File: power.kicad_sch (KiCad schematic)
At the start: 57 parts, among them J4 USB_C_Receptacle_USB2.0_16P, Q5 AO3401A, Q6 2N7002, SW1 SW_Push, U10 BQ27441DRZR-G1A, U5 XL4005, U6 IP5306, U8 FP6298XR, U9 AMS1117-3.3

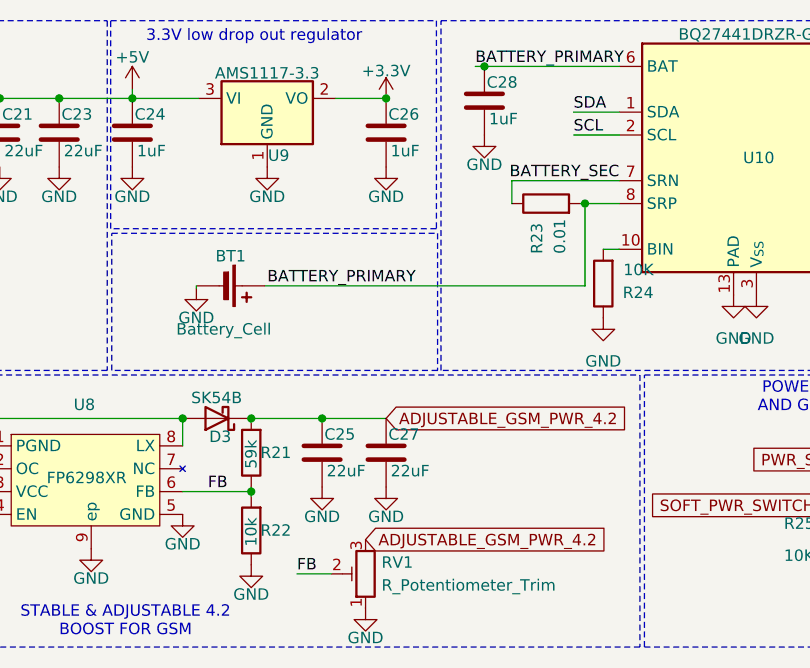
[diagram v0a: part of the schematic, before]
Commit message: cleaned up more routing and component placement
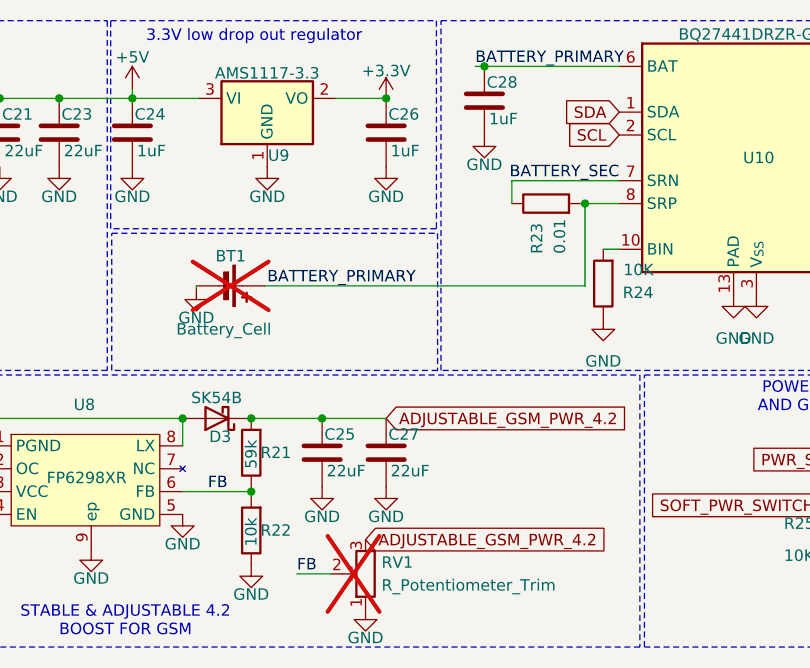
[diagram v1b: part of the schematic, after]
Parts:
- BT1, RV1: now not fitted
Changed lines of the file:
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@@
 	(wire
 		(pts
-			(xy 219.202 22.352) (xy 224.282 22.352)
-		)
-		(stroke
-			(width 0)
-			(type default)
-		)
-	)
-	(wire
-		(pts
 			(xy 132.842 64.77) (xy 132.842 61.976)
 		)
@@
 	(wire
 		(pts
-			(xy 219.202 24.892) (xy 224.282 24.892)
-		)
-		(stroke
-			(width 0)
-			(type default)
-		)
-	)
-	(wire
-		(pts
 			(xy 253.238 60.96) (xy 255.016 60.96)
 		)
@@
 		)
 	)
-	(label "SDA"
-		(at 219.202 22.352 0)
-		(effects
-			(font
-				(size 1.27 1.27)
-			)
-			(justify left bottom)
-		)
-	)
 	(label "VIN"
 		(at 83.058 20.828 0)
@@
 		)
 	)
-	(label "SCL"
-		(at 219.202 24.892 0)
-		(effects
-			(font
-				(size 1.27 1.27)
-			)
-			(justify left bottom)
-		)
-	)
 	(label "BATTERY_PRIMARY"
 		(at 208.28 17.272 0)
@@
 		)
 	)
+	(global_label "SDA"
+		(shape input)
+		(at 224.282 22.352 180)
+		(fields_autoplaced yes)
+		(effects
+			(font
+				(size 1.27 1.27)
+			)
+			(justify right)
+		)
+		(property "Intersheetrefs" "${INTERSHEET_REFS}"
+			(at 217.7287 22.352 0)
+			(effects
+				(font
+					(size 1.27 1.27)
+				)
+				(justify right)
+				(hide yes)
+			)
+		)
+	)
 	(global_label "GSM_PWR_EN"
 		(shape input)
@@
 		)
 	)
+	(global_label "SCL"
+		(shape input)
+		(at 224.282 24.892 180)
+		(fields_autoplaced yes)
+		(effects
+			(font
+				(size 1.27 1.27)
+			)
+			(justify right)
+		)
+		(property "Intersheetrefs" "${INTERSHEET_REFS}"
+			(at 217.7892 24.892 0)
+			(effects
+				(font
+					(size 1.27 1.27)
+				)
+				(justify right)
+				(hide yes)
+			)
+		)
+	)
 	(global_label "CC1"
 		(shape input)
@@
 		(exclude_from_sim yes)
 		(in_bom no)
-		(on_board yes)
+		(on_board no)
 		(dnp no)
 		(fields_autoplaced yes)
@@
 		(exclude_from_sim yes)
 		(in_bom no)
-		(on_board yes)
+		(on_board no)
 		(dnp no)
 		(fields_autoplaced yes)
@@
 		(exclude_from_sim no)
 		(in_bom yes)
-		(on_board yes)
-		(dnp no)
+		(on_board no)
+		(dnp yes)
 		(fields_autoplaced yes)
 		(property "Reference" "RV1"
@@
 		(exclude_from_sim yes)
 		(in_bom no)
-		(on_board yes)
+		(on_board no)
 		(dnp no)
 		(fields_autoplaced yes)
@@
 		(exclude_from_sim yes)
 		(in_bom no)
-		(on_board yes)
+		(on_board no)
 		(dnp no)
 		(fields_autoplaced yes)
@@
 		(exclude_from_sim no)
 		(in_bom yes)
-		(on_board yes)
-		(dnp no)
+		(on_board no)
+		(dnp yes)
 		(property "Reference" "BT1"
 			(at 181.102 38.354 90)

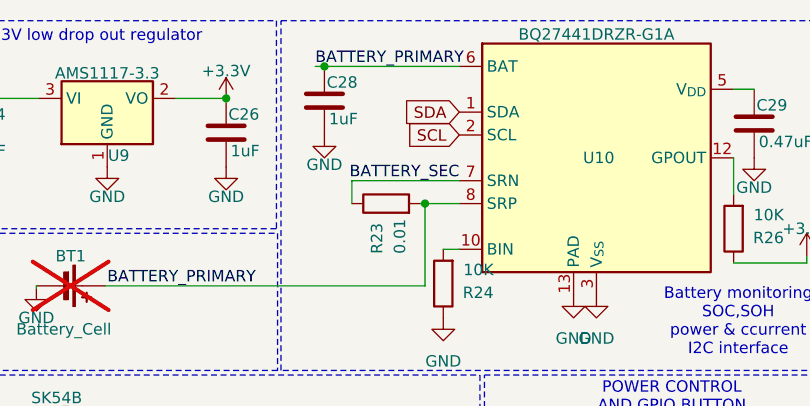
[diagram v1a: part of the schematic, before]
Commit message: added 3.3v logic level  shifting for battery monitoring chip I2C lines
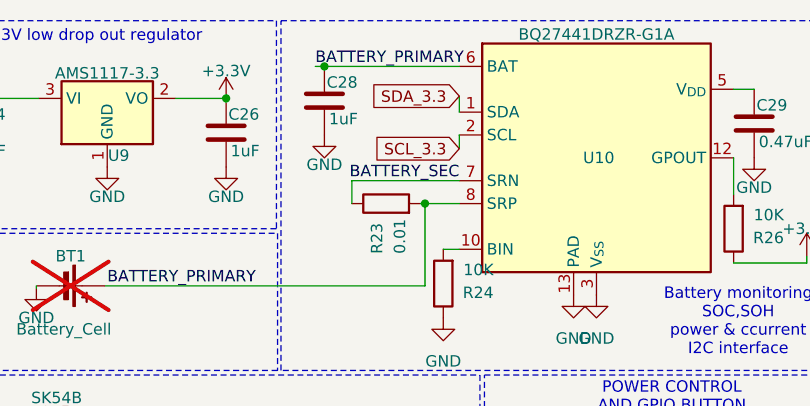
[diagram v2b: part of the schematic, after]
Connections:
- net SCL renamed SCL_3.3
- net SDA renamed SDA_3.3
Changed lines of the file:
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@@
+	(wire
+		(pts
+			(xy 224.282 26.416) (xy 224.282 24.892)
+		)
+		(stroke
+			(width 0)
+			(type default)
+		)
+	)
 	(wire
 		(pts
@@
 		(pts
 			(xy 177.292 41.656) (xy 177.292 41.91)
+		)
+		(stroke
+			(width 0)
+			(type default)
+		)
+	)
+	(wire
+		(pts
+			(xy 224.282 20.574) (xy 224.282 22.352)
 		)
 		(stroke
@@
 		)
 	)
-	(global_label "SDA"
-		(shape input)
-		(at 224.282 22.352 180)
+	(global_label "SDA_3.3"
+		(shape input)
+		(at 224.282 20.574 180)
 		(fields_autoplaced yes)
 		(effects
@@
 		)
 		(property "Intersheetrefs" "${INTERSHEET_REFS}"
-			(at 217.7287 22.352 0)
+			(at 213.7373 20.574 0)
 			(effects
 				(font
@@
 		)
 	)
-	(global_label "SCL"
-		(shape input)
-		(at 224.282 24.892 180)
+	(global_label "SCL_3.3"
+		(shape input)
+		(at 224.282 26.416 180)
 		(fields_autoplaced yes)
 		(effects
@@
 		)
 		(property "Intersheetrefs" "${INTERSHEET_REFS}"
-			(at 217.7892 24.892 0)
-			(effects
-				(font
+			(at 213.7978 26.416 0)
+			(effects
+				(font

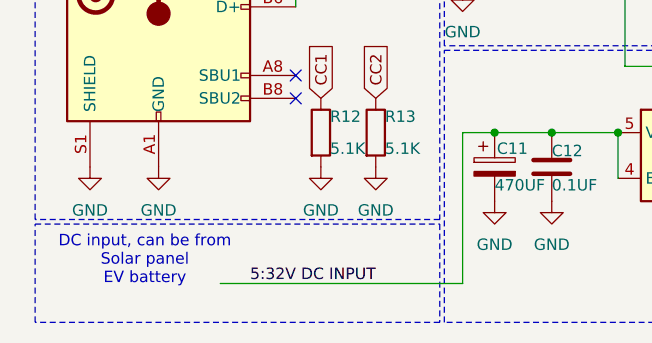
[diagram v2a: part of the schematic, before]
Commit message: added another pin for power connection
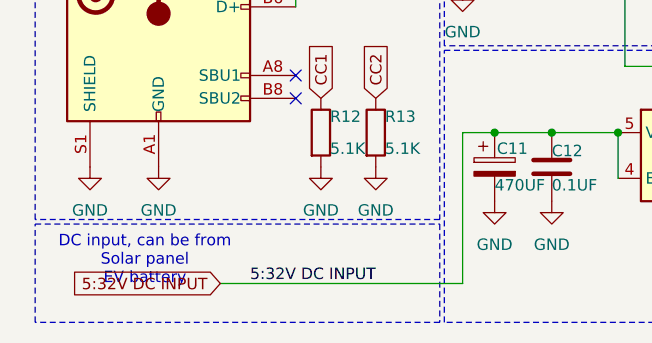
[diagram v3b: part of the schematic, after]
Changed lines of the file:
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@@
+	(wire
+		(pts
+			(xy 32.766 77.47) (xy 59.69 77.47)
+		)
+		(stroke
+			(width 1)
+			(type default)
+			(color 132 0 0 1)
+		)
+	)
 	(wire
 		(pts
@@
 			(width 0)
 			(type default)
-		)
-	)
-	(wire
-		(pts
-			(xy 59.69 77.47) (xy 32.766 77.47)
-		)
-		(stroke
-			(width 1)
-			(type default)
-			(color 132 0 0 1)
 		)
 	)
@@
 			(effects
 				(font
+					(size 1.27 1.27)
+				)
+				(justify right)
+				(hide yes)
+			)
+		)
+	)
+	(global_label "5:32V DC INPUT"
+		(shape input)
+		(at 32.766 77.47 180)
+		(fields_autoplaced yes)
+		(effects
+			(font
+				(size 1.27 1.27)
+			)
+			(justify right)
+		)
+		(property "Intersheetrefs" "${INTERSHEET_REFS}"
+			(at 14.4803 77.47 0)
+			(effects
+				(font
